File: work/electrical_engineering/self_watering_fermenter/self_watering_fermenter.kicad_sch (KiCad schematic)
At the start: 0 parts

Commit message: first cut of schematic
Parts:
- added A1: RaspberryPi_Pico, Module:RaspberryPi_Pico_Common_Unspecified, symbol MCU_Module:RaspberryPi_Pico
- added C1, C2, C3, C4, C5, C6: C, symbol Device:C
- added D1, D3: 1N4004, Diode_THT:D_DO-41_SOD81_P10.16mm_Horizontal, symbol Diode:1N4004
- added D2: D_Schottky, symbol Device:D_Schottky
- added J1: Jack-DC, symbol Connector:Jack-DC
- added M1: Motor_DC, symbol Motor:Motor_DC
- added Q1: IRLB8721PBF, Package_TO_SOT_THT:TO-220-3_Vertical, symbol Transistor_FET:IRLB8721PBF
- added R1: 959, symbol Device:R_US
- added R2, R4: 240, symbol Device:R_US
- added R3: 632.6, symbol Device:R_US
- added R5, R6, R7: R_US, symbol Device:R_US
- added SW1: SW_SPDT, symbol Switch:SW_SPDT
- added U1, U2: LM317_TO-220, Package_TO_SOT_THT:TO-220-3_Vertical, symbol Regulator_Linear:LM317_TO-220
- added U3: 74AHCT125, symbol 74xx:74AHCT125
- added U4: SFH900, OptoDevice:Siemens_SFH900, symbol Sensor_Proximity:SFH900
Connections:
- new net: C4.1, D3.2 (A), M1.1 (+), U1.2 (VO)
- new net: D3.1 (K), M1.2 (-), Q1.2 (D)
- new net: U3.2, U4.2 (K)
- new net: J1.1, SW1.2 (B)
- new net: C5.1, R4.2
- new net: C3.1, R2.2
- new net: R7.1, U3.1
- new net: R1.1, R2.1, U1.1 (ADJ)
- new net: C1.1, C2.1, D1.1 (K), U1.3 (VI), U2.3 (VI)
- new net: R3.1, R4.1, U2.1 (ADJ)
- new net: C6.1, U2.2 (VO)
- new net: D1.2 (A), SW1.1 (A)
- new net: A1.1 (GPIO0), R5.1, R6.2
- new net: A1.40 (VBUS), D2.1 (K)
- new net: Q1.1 (G), R6.1
- new net: A1.13 (GND), A1.18 (GND), A1.23 (GND), A1.28 (GND), A1.3 (GND), A1.38 (GND), A1.8 (GND)
- new net: A1.4 (GPIO2), U3.3
- new net GND: A1.39 (VSYS), C1.2, C2.2, C3.2, C4.2, C5.2, C6.2, J1.2, Q1.3 (S), R1.2, R3.2, R5.2, R7.2, U4.3 (C)
- no-connect marks 0 -> 30
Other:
- note added: "signal! from liquid level sensor 4.5V Green D2"

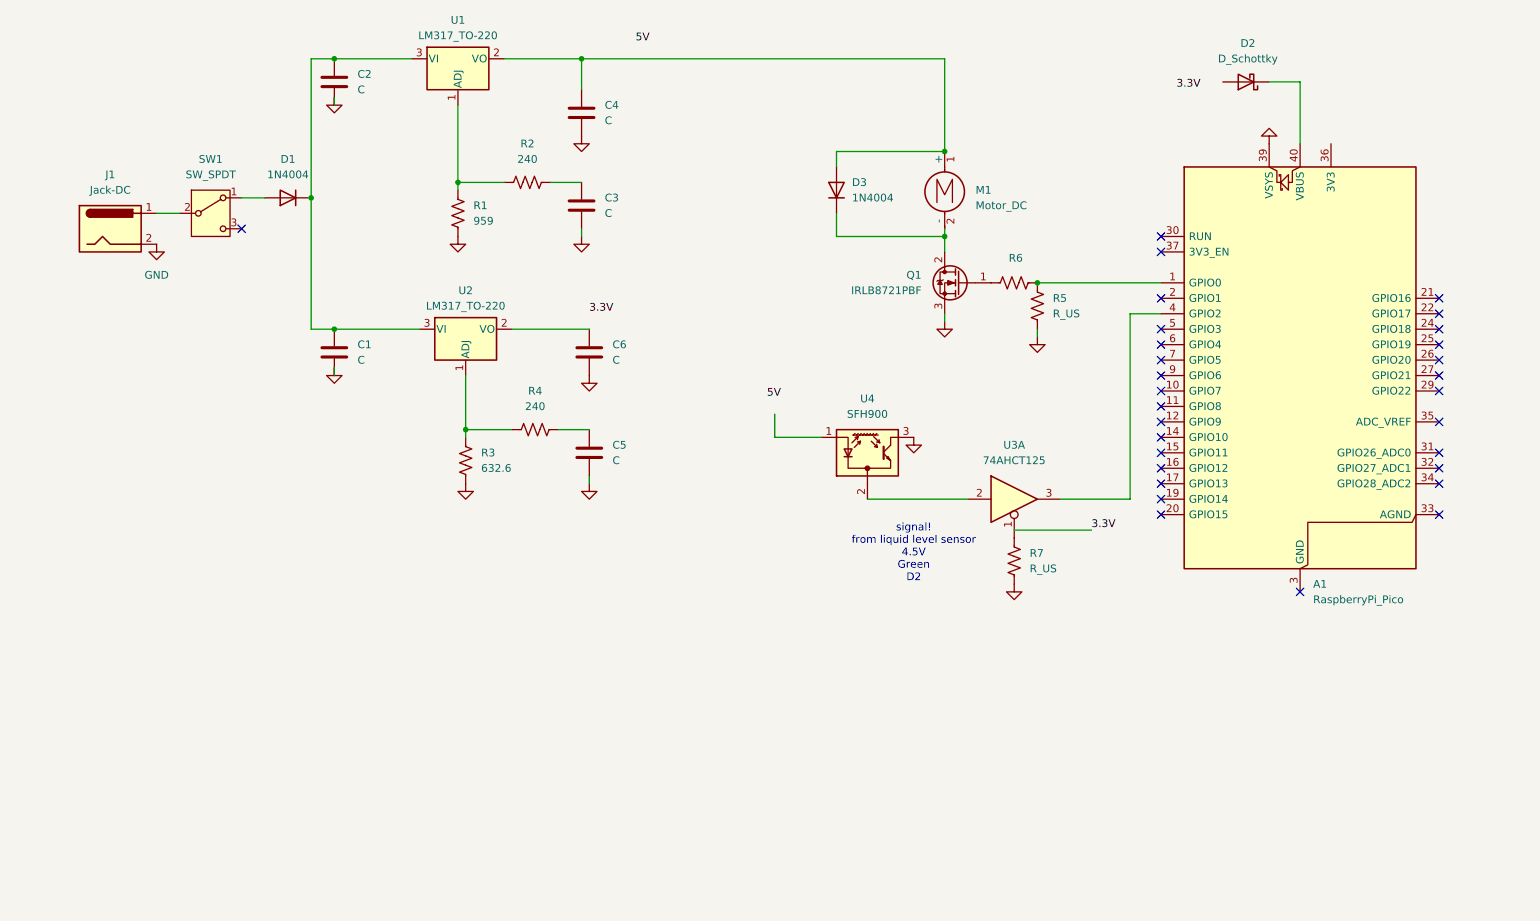
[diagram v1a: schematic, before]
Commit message: added custom symbol for the liquid level sensor
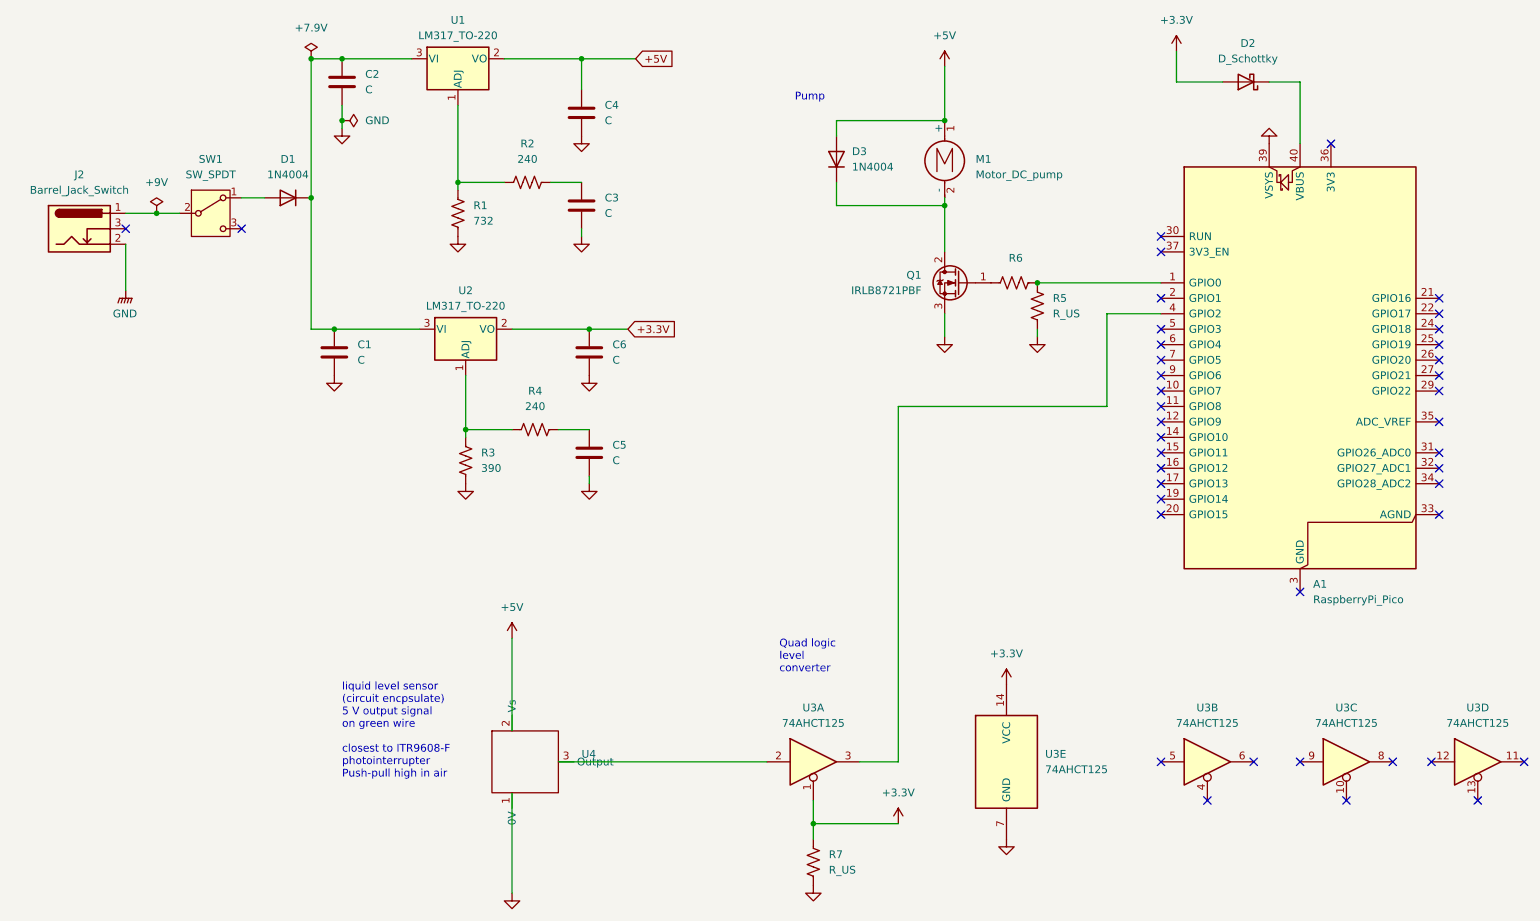
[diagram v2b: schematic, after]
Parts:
- removed J1: Jack-DC, symbol Connector:Jack-DC
- removed U4: SFH900, OptoDevice:Siemens_SFH900, symbol Sensor_Proximity:SFH900
- added J2: Barrel_Jack_Switch, symbol Connector:Barrel_Jack_Switch
- added unit 4 of U3
- added unit 2 of U3
- added unit 5 of U3
- added unit 3 of U3
- added U4: ~, symbol New_Library:_2
- M1: value Motor_DC -> Motor_DC_pump
- R1: value 959 -> 732
- R3: value 632.6 -> 390
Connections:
- net GND: now also J2.2, U3.7 (GND), U4.1 (0V)
- net +5V: now reaches C4.1, D3.2 (A), M1.1 (+), U1.2 (VO)
- net +5V: now also U4.2 (Vs)
- net at U3.2: now also U4.3 (Output)
- net at SW1.2 (B): now also J2.1
- net +3.3V: now reaches R7.1, U3.1
- net +3.3V: now also C6.1, D2.2 (A), U2.2 (VO), U3.14 (VCC)
- no-connect marks 30 -> 41
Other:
- note added: "Pump"
- note added: "Quad logic level converter"
- note added: "liquid level sensor (circuit encpsulate) 5 V output signal on green wire closest to ITR9608-F photointerrupter Push-pull high in air"
- note removed: "signal! from liquid level sensor 4.5V Green D2"
- title: (none) -> Self Watering Fermenter
- moved on the sheet: D3, M1, R7, U3A

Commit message: Soldered and working
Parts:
- removed D1: 1N4004, Diode_THT:D_DO-41_SOD81_P10.16mm_Horizontal, symbol Diode:1N4004
- removed D2: D_Schottky, symbol Device:D_Schottky
- C1, C2: value C -> 0.1 uF
- C3, C5: value C -> 10 uF
- C4, C6: value C -> 1 uF
- R1: value 732 -> 732 Ω
- R2, R4: value 240 -> 240 Ω
- R3: value 390 -> 390 Ω
- R5: value R_US -> 100 kΩ
- R6: value R_US -> 1 kΩ
- R7: value R_US -> 10 kΩ
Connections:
- net +3.3V: now also A1.39 (VSYS)
- net GND: no longer A1.39 (VSYS)
- net at C1.1, C2.1, U1.3 (VI)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: now also SW1.1 (A)
- no-connect marks 41 -> 42
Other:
- note added: "Quad digital buffer and logic level converter"
- note removed: "Quad logic level converter"

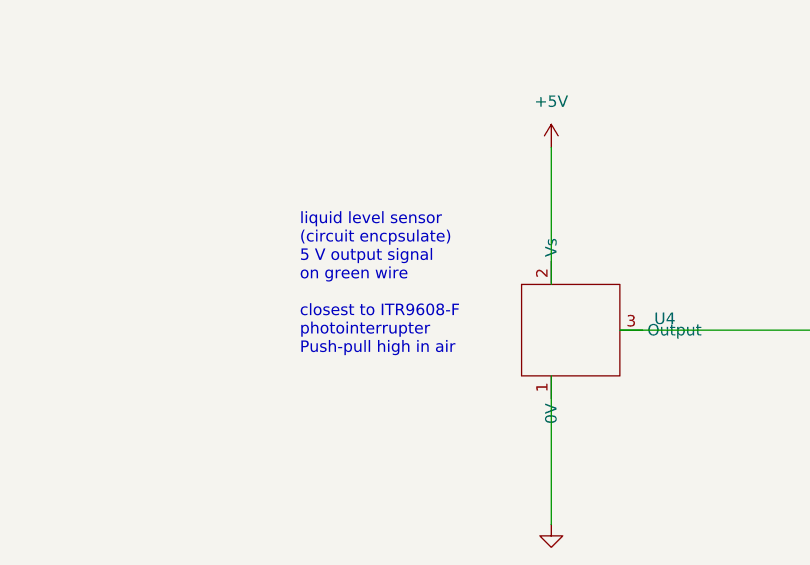
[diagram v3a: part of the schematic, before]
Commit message: simplified block diagram for using power mosfet
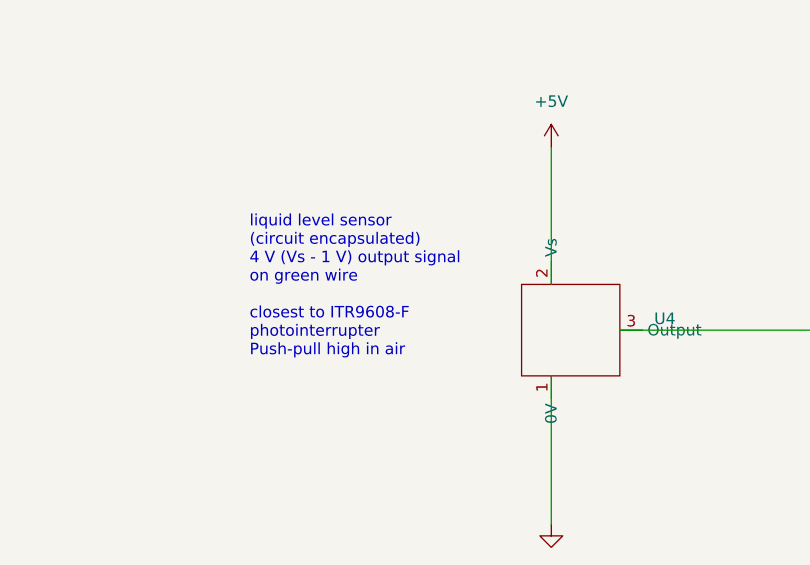
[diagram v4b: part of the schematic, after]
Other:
- note added: "liquid level sensor (circuit encapsulated) 4 V (Vs - 1 V) output signal on green wire closest to ITR9608-F photointerrupter Push-pull high in air"
- note removed: "liquid level sensor (circuit encpsulate) 5 V output signal on green wire closest to ITR9608-F photointerrupter Push-pull high in air"
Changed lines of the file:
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@@
 		)
 	)
-	(text "liquid level sensor\n(circuit encpsulate)\n5 V output signal \non green wire\n\nclosest to ITR9608-F\nphotointerrupter\nPush-pull high in air"
+	(text "liquid level sensor\n(circuit encapsulated)\n4 V (Vs - 1 V) output signal \non green wire\n\nclosest to ITR9608-F\nphotointerrupter\nPush-pull high in air"
 		(exclude_from_sim no)
-		(at 66.04 134.62 0)
+		(at 60.452 134.874 0)
 		(effects
 			(font
@@
 		(polyline
 			(pts
-				(xy 64.135 124.46) (xy 64.135 154.94) (xy 126.365 154.94) (xy 126.365 124.46)
+				(xy 58.42 124.46) (xy 58.42 154.94) (xy 125.095 154.94) (xy 125.095 124.46)
 			)
 			(stroke
